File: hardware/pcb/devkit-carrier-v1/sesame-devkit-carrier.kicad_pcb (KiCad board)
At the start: 2 copper layers, 69 x 42 mm, 28 parts, among them J1 DevKit L, J2 DevKit R, J3 OLED, J4 IO, J5 IO2, J6 Battery pigtail, SW1 Switch, U1 Pololu D24V50F5

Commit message: Carrier PCB: widen C3 pad gap to 0.8 mm, route battery-sense tap away from socket pins
Short-risk analysis found the two worst spots: C3's pads (battery + to GND)
were 0.40 mm apart, and the 12.6 V sense tap passed 0.22 mm from D13
between socket pins. C3 pads narrowed along the pitch (gap 0.80 mm, now
the board minimum); sense tap runs from C3 between the socket rows to R1.
ERC/DRC/parity/audit clean, kicad-happy unchanged.

Co-Authored-By: Claude Opus 5.5 <noreply@anthropic.com>
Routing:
- net VBAT_SW: track 64.1 -> 50.0 mm

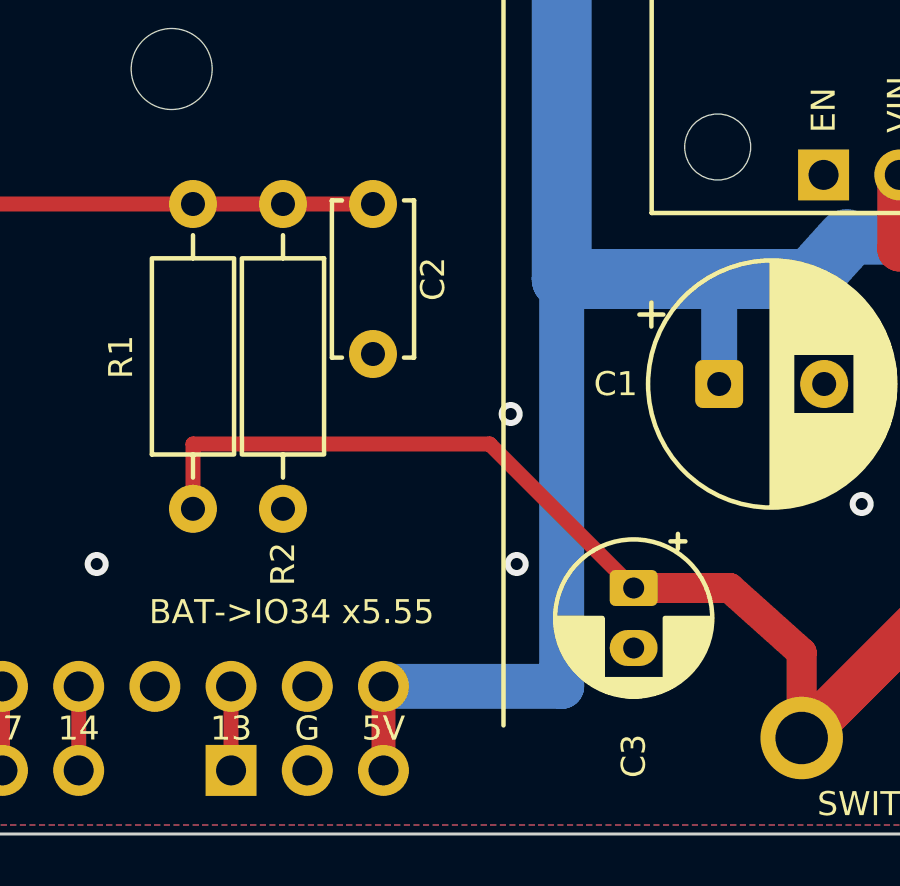
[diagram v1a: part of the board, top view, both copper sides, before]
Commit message: Carrier PCB: wider short-risk margins and a short_check.py gate
Ground fill 0.5 mm back from all copper (was 0.3), C3 on 2.5 mm pitch
with narrowed pads (1.3 mm gap across the battery), R1/R2 battery-to-GND
pads 2.2 mm apart, stitching vias moved off the 5V feed. short_check.py
(plain Python, no KiCad) enforces the margins. ERC/DRC/parity/audit clean,
kicad-happy unchanged.

Co-Authored-By: Claude Opus 5.5 <noreply@anthropic.com>
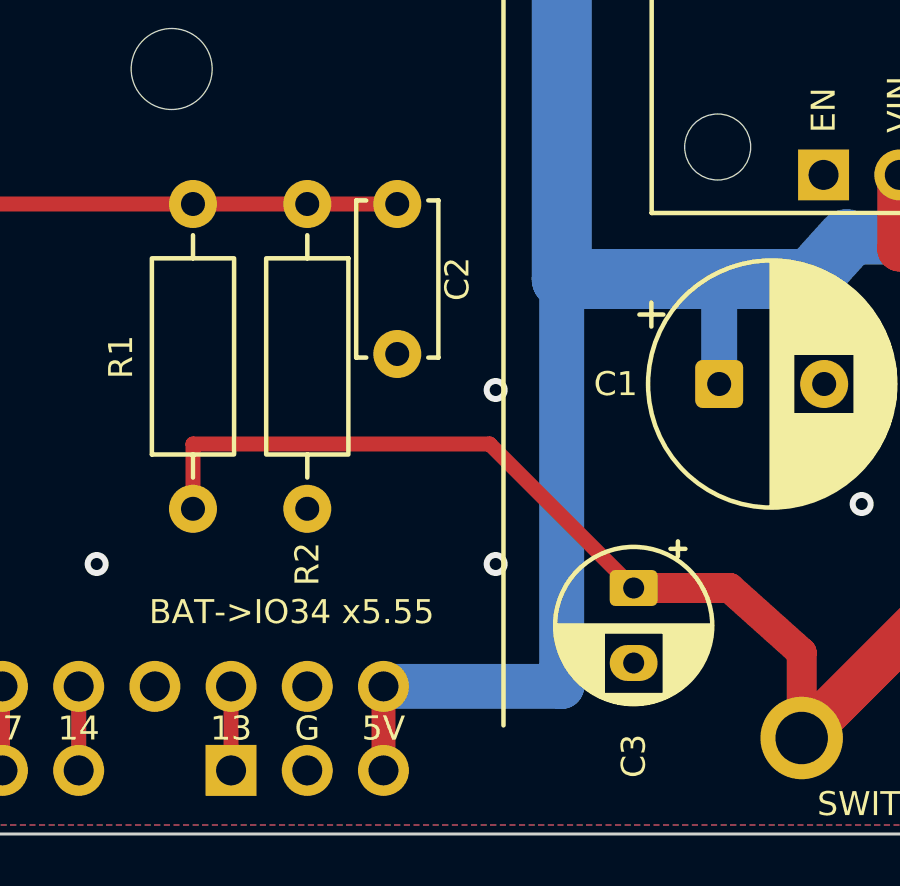
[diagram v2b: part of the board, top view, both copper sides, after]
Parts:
- C3: footprint Sesame:CP_Radial_D5.0mm_P2.00mm -> Sesame:CP_Radial_D5.0mm_P2.50mm
- moved C2 0.81 mm to (38.5, 21.0)
- moved R2 0.81 mm to (35.5, 21.0)
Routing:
- net BAT_SENSE: track 43.7 -> 44.5 mm
